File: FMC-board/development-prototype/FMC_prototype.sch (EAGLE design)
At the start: 56 parts, among them J1 DC_POWER_JACK-PJ-102AH, J2 DC_POWER_JACK-PJ-102AH

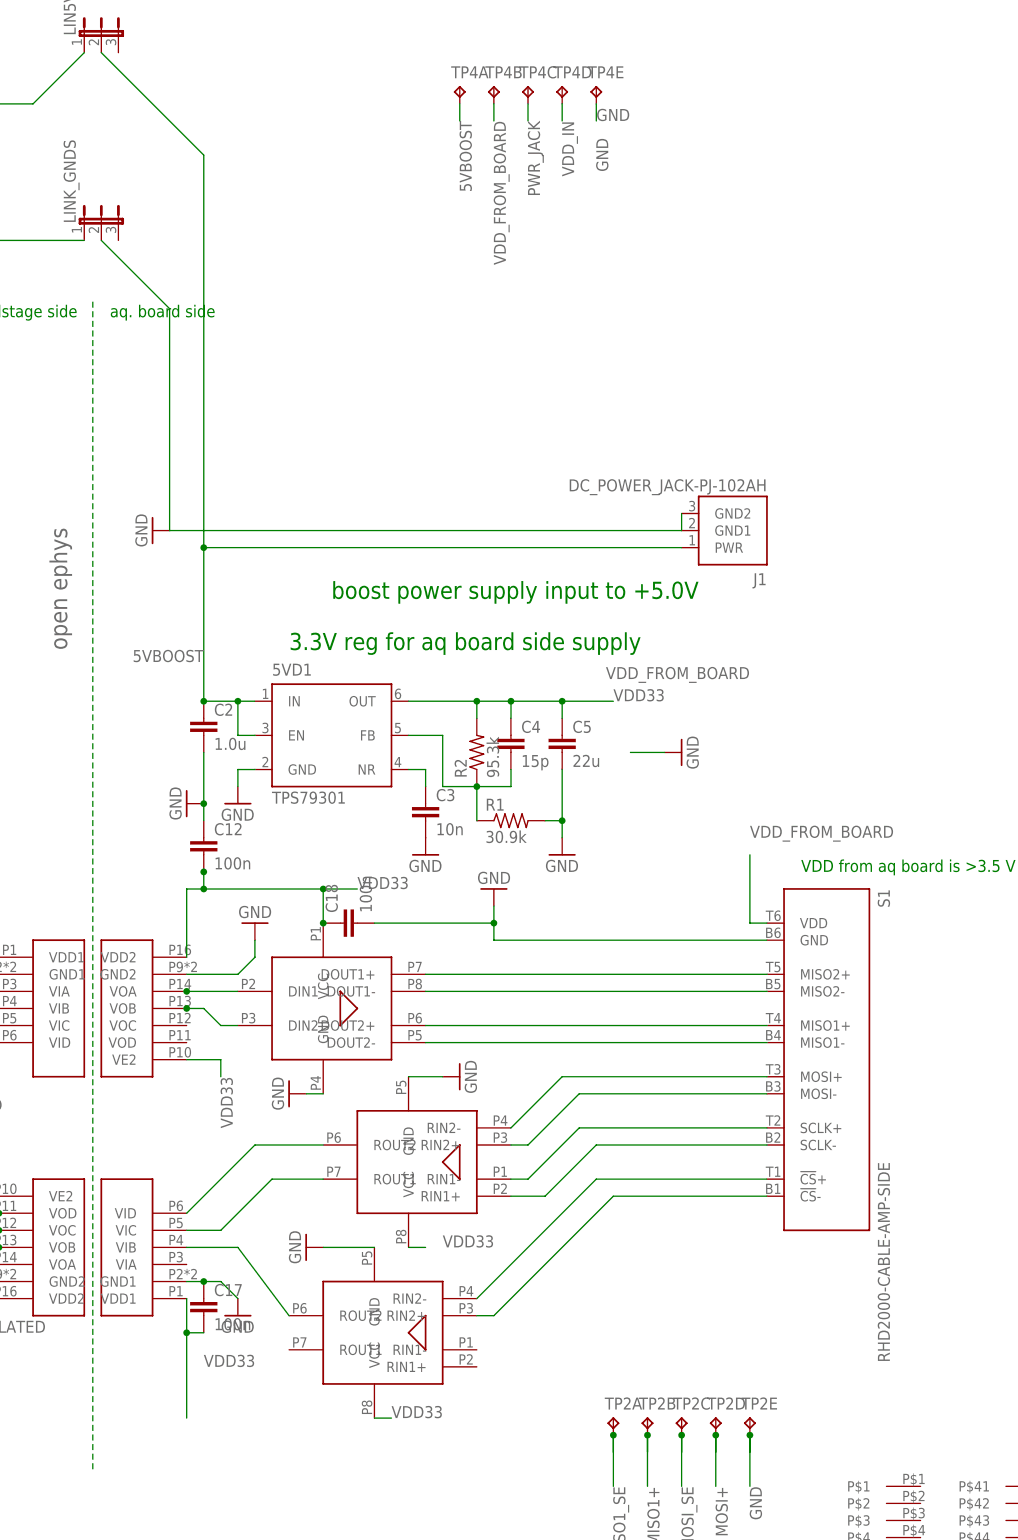
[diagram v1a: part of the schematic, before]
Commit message: initial board layout fpga side
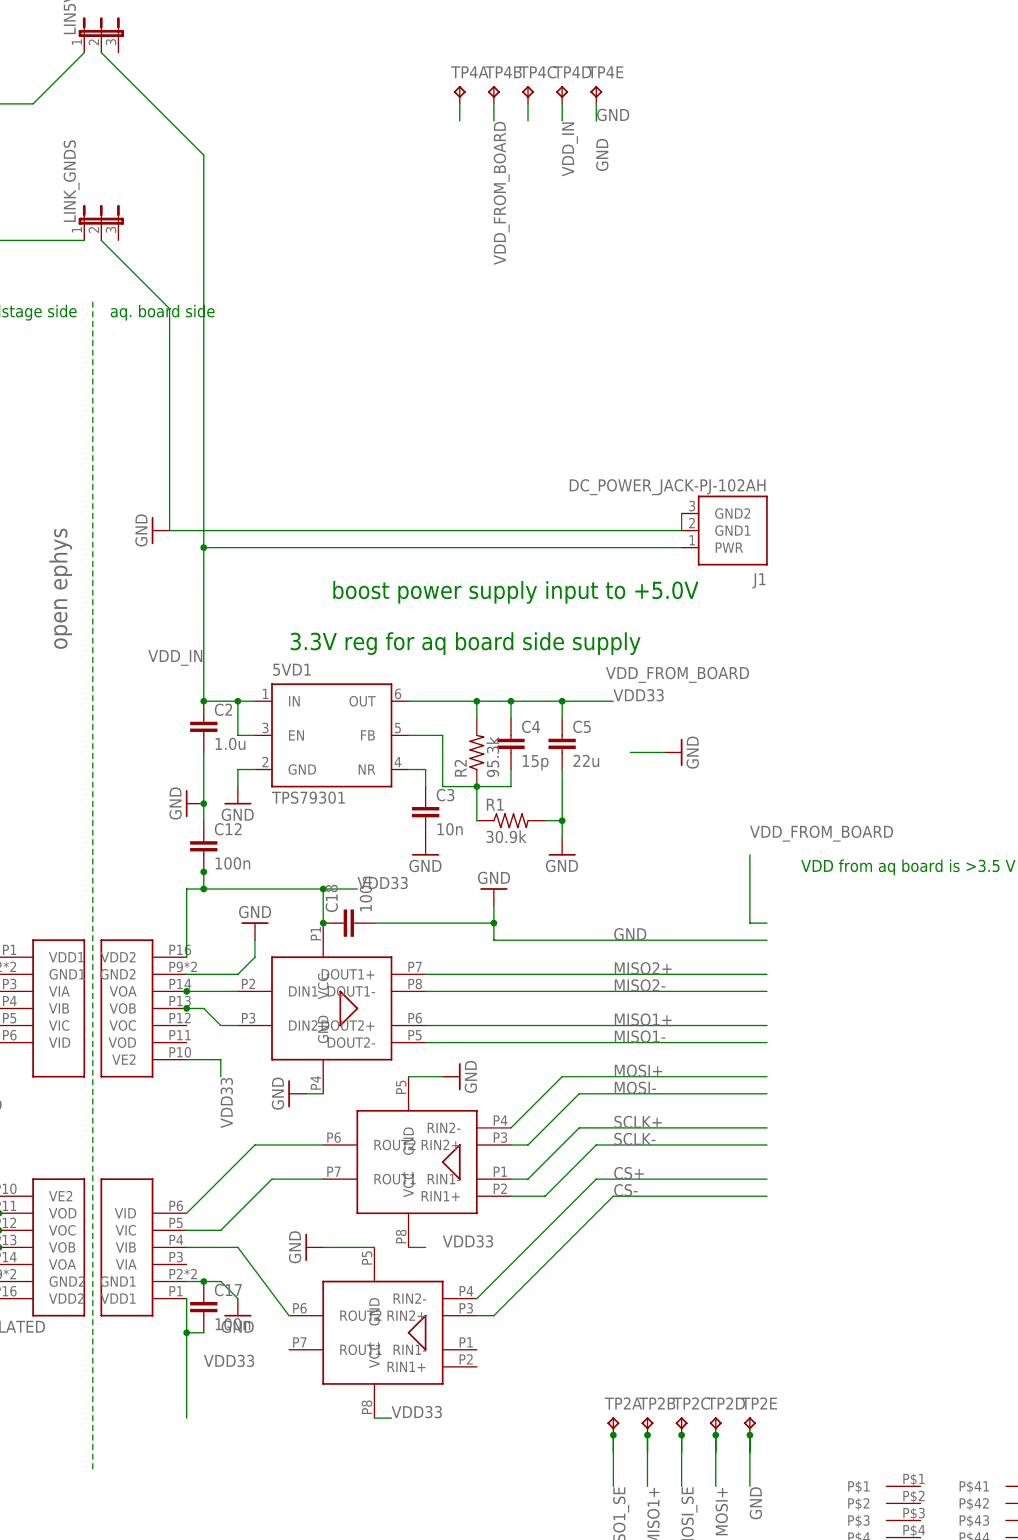
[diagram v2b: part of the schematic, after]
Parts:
- removed S1: RHD2000-CABLE-AMP-SIDE, RHD2000:RHD2000-CABLE-AMP-SIDE
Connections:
- net 5VBOOST: no longer 5VD1.EN, 5VD1.IN, C2.1, J1.PWR, LIN5V.2
- net CS+: no longer S1.!CS!+
- net CS-: no longer S1.!CS!-
- net GND: no longer S1.GND
- net MISO1+: no longer S1.MISO1+
- net MISO1-: no longer S1.MISO1-
- net MISO2+: no longer S1.MISO2+
- net MISO2-: no longer S1.MISO2-
- net MOSI+: no longer S1.MOSI+
- net MOSI-: no longer S1.MOSI-
- net SCLK+: no longer S1.SCLK+
- net SCLK-: no longer S1.SCLK-
- net VDD_FROM_BOARD: no longer S1.VDD
- net VDD_IN: now also 5VD1.EN, 5VD1.IN, C2.1, J1.PWR, LIN5V.2
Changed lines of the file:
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@@
 <part name="U$5" library="SA_BB" deviceset="SMA_JACK_142-0701-201_DEV" device=""/>
 <part name="GND6" library="supply1" deviceset="GND" device=""/>
-<part name="S1" library="RHD2000" deviceset="RHD2000-CABLE-AMP-SIDE" device=""/>
 <part name="U$1" library="open-ephys" deviceset="OPEN_EPHYS_LOGO" device=""/>
 <part name="U$3" library="open-ephys" deviceset="ADN4663" device=""/>
@@
 <instance part="U$5" gate="G$1" x="175.26" y="109.22"/>
 <instance part="GND6" gate="1" x="193.04" y="203.2" rot="R270"/>
-<instance part="S1" gate="A" x="271.78" y="208.28" rot="R90"/>
 <instance part="U$1" gate="G$1" x="160.02" y="269.24" rot="R90"/>
 <instance part="U$3" gate="G$1" x="203.2" y="210.82"/>
@@
 <net name="MISO2+" class="0">
 <segment>
-<pinref part="S1" gate="A" pin="MISO2+"/>
 <pinref part="U$3" gate="G$1" pin="DOUT1+"/>
 <wire x1="213.36" y1="220.98" x2="264.16" y2="220.98" width="0.1524" layer="91"/>
+<label x="241.3" y="220.98" size="1.778" layer="95"/>
 </segment>
 </net>
 <net name="MISO2-" class="0">
 <segment>
-<pinref part="S1" gate="A" pin="MISO2-"/>
 <pinref part="U$3" gate="G$1" pin="DOUT1-"/>
 <wire x1="213.36" y1="218.44" x2="264.16" y2="218.44" width="0.1524" layer="91"/>
+<label x="241.3" y="218.44" size="1.778" layer="95"/>
 </segment>
 </net>
 <net name="MISO1+" class="0">
 <segment>
-<pinref part="S1" gate="A" pin="MISO1+"/>
 <pinref part="U$3" gate="G$1" pin="DOUT2+"/>
 <wire x1="213.36" y1="213.36" x2="264.16" y2="213.36" width="0.1524" layer="91"/>
+<label x="241.3" y="213.36" size="1.778" layer="95"/>
 </segment>
 <segment>
@@
 <net name="MISO1-" class="0">
 <segment>
-<pinref part="S1" gate="A" pin="MISO1-"/>
 <pinref part="U$3" gate="G$1" pin="DOUT2-"/>
 <wire x1="213.36" y1="210.82" x2="264.16" y2="210.82" width="0.1524" layer="91"/>
+<label x="241.3" y="210.82" size="1.778" layer="95"/>
 </segment>
 </net>
@@
 <net name="SCLK-" class="0">
 <segment>
-<pinref part="S1" gate="A" pin="SCLK-"/>
 <wire x1="226.06" y1="187.96" x2="231.14" y2="187.96" width="0.1524" layer="91"/>
 <wire x1="231.14" y1="187.96" x2="238.76" y2="195.58" width="0.1524" layer="91"/>
 <wire x1="238.76" y1="195.58" x2="264.16" y2="195.58" width="0.1524" layer="91"/>
 <pinref part="U$8" gate="G$1" pin="RIN1+"/>
+<label x="241.3" y="195.58" size="1.778" layer="95"/>
 </segment>
 </net>
 <net name="SCLK+" class="0">
 <segment>
-<pinref part="S1" gate="A" pin="SCLK+"/>
 <wire x1="226.06" y1="190.5" x2="228.6" y2="190.5" width="0.1524" layer="91"/>
 <wire x1="228.6" y1="190.5" x2="236.22" y2="198.12" width="0.1524" layer="91"/>
 <wire x1="236.22" y1="198.12" x2="264.16" y2="198.12" width="0.1524" layer="91"/>
 <pinref part="U$8" gate="G$1" pin="RIN1-"/>
+<label x="241.3" y="198.12" size="1.778" layer="95"/>
 </segment>
 </net>
 <net name="MOSI-" class="0">
 <segment>
-<pinref part="S1" gate="A" pin="MOSI-"/>
 <wire x1="226.06" y1="195.58" x2="228.6" y2="195.58" width="0.1524" layer="91"/>
 <wire x1="228.6" y1="195.58" x2="236.22" y2="203.2" width="0.1524" layer="91"/>
 <wire x1="236.22" y1="203.2" x2="264.16" y2="203.2" width="0.1524" layer="91"/>
 <pinref part="U$8" gate="G$1" pin="RIN2+"/>
+<label x="241.3" y="203.2" size="1.778" layer="95"/>
 </segment>
 </net>
 <net name="MOSI+" class="0">
 <segment>
-<pinref part="S1" gate="A" pin="MOSI+"/>
 <wire x1="226.06" y1="198.12" x2="233.68" y2="205.74" width="0.1524" layer="91"/>
 <wire x1="233.68" y1="205.74" x2="264.16" y2="205.74" width="0.1524" layer="91"/>
 <pinref part="U$8" gate="G$1" pin="RIN2-"/>
+<label x="241.3" y="205.74" size="1.778" layer="95"/>
 </segment>
 <segment>
@@
 <net name="CS-" class="0">
 <segment>
-<pinref part="S1" gate="A" pin="!CS!-"/>
 <wire x1="220.98" y1="170.18" x2="223.52" y2="170.18" width="0.1524" layer="91"/>
 <wire x1="223.52" y1="170.18" x2="241.3" y2="187.96" width="0.1524" layer="91"/>
 <wire x1="241.3" y1="187.96" x2="264.16" y2="187.96" width="0.1524" layer="91"/>
 <pinref part="U$10" gate="G$1" pin="RIN2+"/>
+<label x="241.3" y="187.96" size="1.778" layer="95"/>
 </segment>
 </net>
 <net name="CS+" class="0">
 <segment>
-<pinref part="S1" gate="A" pin="!CS!+"/>
 <wire x1="220.98" y1="172.72" x2="238.76" y2="190.5" width="0.1524" layer="91"/>
 <wire x1="238.76" y1="190.5" x2="264.16" y2="190.5" width="0.1524" layer="91"/>
 <pinref part="U$10" gate="G$1" pin="RIN2-"/>
+<label x="241.3" y="190.5" size="1.778" layer="95"/>
 </segment>
 </net>
@@
 </segment>
 <segment>
-<pinref part="S1" gate="A" pin="GND"/>
 <pinref part="GND5" gate="1" pin="GND"/>
 <wire x1="223.52" y1="231.14" x2="223.52" y2="228.6" width="0.1524" layer="91"/>
@@
 <wire x1="205.74" y1="228.6" x2="223.52" y2="228.6" width="0.1524" layer="91"/>
 <junction x="223.52" y="228.6"/>
+<label x="241.3" y="226.06" size="1.778" layer="95"/>
 </segment>
 <segment>
@@
 <label x="233.68" y="347.98" size="1.778" layer="95" rot="R270"/>
 </segment>
-</net>
-<net name="5VBOOST" class="0">
 <segment>
 <wire x1="251.46" y1="284.48" x2="180.34" y2="284.48" width="0.1524" layer="91"/>
@@
 <junction x="180.34" y="284.48"/>
 </segment>
+</net>
+<net name="5VBOOST" class="0">
 <segment>
 <pinref part="TP4" gate="A" pin="TP"/>
 <wire x1="218.44" y1="350.52" x2="218.44" y2="347.98" width="0.1524" layer="91"/>
-<label x="218.44" y="347.98" size="1.778" layer="95" rot="R270"/>
 </segment>
 </net>
@@
 <pinref part="TP4" gate="C" pin="TP"/>
 <wire x1="228.6" y1="350.52" x2="228.6" y2="347.98" width="0.1524" layer="91"/>
-<label x="228.6" y="347.98" size="1.778" layer="95" rot="R270"/>
 </segment>
 </net>
 <net name="VDD_FROM_BOARD" class="0">
 <segment>
-<pinref part="S1" gate="A" pin="VDD"/>
 <wire x1="264.16" y1="228.6" x2="261.62" y2="228.6" width="0.1524" layer="91"/>
 <wire x1="261.62" y1="228.6" x2="261.62" y2="238.76" width="0.1524" layer="91"/>

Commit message: more placement and labels
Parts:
- renumbered LIN5V to LINK-5V
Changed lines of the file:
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@@
 <part name="J2" library="RHD2000_eval_board" deviceset="DC_POWER_JACK" device="-PJ-102AH"/>
 <part name="LINK_GNDS" library="jumper" deviceset="JP2E" device=""/>
-<part name="LIN5V" library="jumper" deviceset="JP2E" device=""/>
+<part name="LINK-5V" library="jumper" deviceset="JP2E" device=""/>
 <part name="S2" library="RHD2000_eval_board" deviceset="RHD2000-CABLE-DAQ-SIDE" device=""/>
 <part name="U$13" library="SA_BB" deviceset="SMA_JACK_142-0701-201_DEV" device=""/>
@@
 <instance part="J2" gate="A" x="119.38" y="358.14" rot="R270"/>
 <instance part="LINK_GNDS" gate="1" x="165.1" y="332.74"/>
-<instance part="LIN5V" gate="1" x="165.1" y="360.68"/>
+<instance part="LINK-5V" gate="1" x="165.1" y="360.68"/>
 <instance part="S2" gate="A" x="33.02" y="88.9" rot="R270"/>
 <instance part="U$13" gate="G$1" x="175.26" y="71.12"/>
@@
 <wire x1="121.92" y1="289.56" x2="121.92" y2="350.52" width="0.1524" layer="91"/>
 <pinref part="J2" gate="A" pin="PWR"/>
-<pinref part="LIN5V" gate="1" pin="1"/>
+<pinref part="LINK-5V" gate="1" pin="1"/>
 <wire x1="121.92" y1="350.52" x2="154.94" y2="350.52" width="0.1524" layer="91"/>
 <wire x1="154.94" y1="350.52" x2="162.56" y2="358.14" width="0.1524" layer="91"/>
@@
 <wire x1="185.42" y1="256.54" x2="187.96" y2="256.54" width="0.1524" layer="91"/>
 <pinref part="J1" gate="A" pin="PWR"/>
-<pinref part="LIN5V" gate="1" pin="2"/>
+<pinref part="LINK-5V" gate="1" pin="2"/>
 <wire x1="180.34" y1="284.48" x2="180.34" y2="342.9" width="0.1524" layer="91"/>
 <wire x1="180.34" y1="342.9" x2="165.1" y2="358.14" width="0.1524" layer="91"/>
